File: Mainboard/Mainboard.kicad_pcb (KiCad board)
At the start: 2 copper layers, 60 x 84 mm, 27 parts, among them J1 Bus_M.2_Socket_E, J3 USB_A_Stacked, J4 Micro_SD_Card, J6 Conn_01x09_Pin, J7 Conn_01x09_Pin, U1 Hirose DF40C-100DS-0.4V, U2 ADS1115IDGS, U3 PCM5102, U4 PAM8403

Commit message: Second Commit (Test)
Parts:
- moved C4 10.8 mm to (88.8, 117.2)
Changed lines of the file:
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@@
 	(footprint "Capacitor_SMD:C_0201_0603Metric_Pad0.64x0.40mm_HandSolder"
 		(layer "F.Cu")
-		(at 80.156 123.753685)
+		(at 88.8175 117.25)
 		(descr "Capacitor SMD 0201 (0603 Metric), square (rectangular) end terminal, IPC-7351 nominal with elongated pad for handsoldering. (Body size source: https://www.vishay.com/docs/20052/crcw0201e3.pdf), generated with kicad-footprint-generator")
 		(tags "capacitor handsolder")

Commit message: Mini Resistor Update
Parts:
- moved R~{5.1kO}1 143.1 mm to (99.8, 124.9), turned to -90 degrees
- moved R~{5.1kO}2 139.6 mm to (101.5, 124.9), turned to -90 degrees
- moved R4.7kO3 85.4 mm to (146.7, 93.5)
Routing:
- net Net-(USBC_ALTPWR1-CC2): track 0.00 -> 4.41 mm
- net Net-(USBC_ALTPWR1-CC1): track 0.00 -> 4.09 mm
- net GND: track 0.00 -> 1.75 mm
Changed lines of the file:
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@@
 	(footprint "Resistor_SMD:R_0603_1608Metric_Pad0.98x0.95mm_HandSolder"
 		(layer "F.Cu")
-		(at 229.605 69.39)
+		(at 101.5 124.9125 -90)
 		(descr "Resistor SMD 0603 (1608 Metric), square (rectangular) end terminal, IPC-7351 nominal with elongated pad for handsoldering. (Body size source: IPC-SM-782 page 72, https://www.pcb-3d.com/wordpress/wp-content/uploads/ipc-sm-782a_amendment_1_and_2.pdf), generated with kicad-footprint-generator")
 		(tags "resistor handsolder")
 		(property "Reference" "R~{5.1kO}2"
-			(at 0 -1.43 0)
+			(at 2.8375 0 180)
 			(layer "F.SilkS")
 			(effects
@@
 		)
 		(property "Value" "R"
-			(at 0 1.43 0)
+			(at 0 1.43 90)
 			(layer "F.Fab")
+			(hide yes)
 			(effects
 				(font
@@
 		)
 		(property "Datasheet" ""
-			(at 0 0 0)
+			(at 0 0 90)
 			(layer "F.Fab")
 			(hide yes)
@@
 		)
 		(property "Description" "Resistor"
-			(at 0 0 0)
+			(at 0 0 90)
 			(layer "F.Fab")
 			(hide yes)
@@
 		(duplicate_pad_numbers_are_jumpers no)
 		(fp_line
-			(start -0.254724 -0.5225)
-			(end 0.254724 -0.5225)
+			(start -0.254724 0.5225)
+			(end 0.254724 0.5225)
 			(stroke
 				(width 0.12)
@@
 		)
 		(fp_line
-			(start -0.254724 0.5225)
-			(end 0.254724 0.5225)
+			(start -0.254724 -0.5225)
+			(end 0.254724 -0.5225)
 			(stroke
 				(width 0.12)
@@
 		)
 		(fp_line
-			(start -1.65 -0.73)
-			(end 1.65 -0.73)
+			(start -1.65 0.73)
+			(end -1.65 -0.73)
 			(stroke
 				(width 0.05)
@@
 		)
 		(fp_line
-			(start -1.65 0.73)
-			(end -1.65 -0.73)
+			(start 1.65 0.73)
+			(end -1.65 0.73)
 			(stroke
 				(width 0.05)
@@
 		)
 		(fp_line
-			(start 1.65 -0.73)
-			(end 1.65 0.73)
+			(start -1.65 -0.73)
+			(end 1.65 -0.73)
 			(stroke
 				(width 0.05)
@@
 		)
 		(fp_line
-			(start 1.65 0.73)
-			(end -1.65 0.73)
+			(start 1.65 -0.73)
+			(end 1.65 0.73)
 			(stroke
 				(width 0.05)
@@
 		)
 		(fp_line
-			(start -0.8 -0.4125)
-			(end 0.8 -0.4125)
+			(start -0.8 0.4125)
+			(end -0.8 -0.4125)
 			(stroke
 				(width 0.1)
@@
 		)
 		(fp_line
-			(start -0.8 0.4125)
-			(end -0.8 -0.4125)
+			(start 0.8 0.4125)
+			(end -0.8 0.4125)
 			(stroke
 				(width 0.1)
@@
 		)
 		(fp_line
-			(start 0.8 -0.4125)
-			(end 0.8 0.4125)
+			(start -0.8 -0.4125)
+			(end 0.8 -0.4125)
 			(stroke
 				(width 0.1)
@@
 		)
 		(fp_line
-			(start 0.8 0.4125)
-			(end -0.8 0.4125)
+			(start 0.8 -0.4125)
+			(end 0.8 0.4125)
 			(stroke
 				(width 0.1)
@@
 		)
 		(fp_text user "${REFERENCE}"
-			(at 0 0 0)
+			(at 0 0 90)
 			(layer "F.Fab")
 			(effects
@@
 		)
 		(pad "1" smd roundrect
-			(at -0.9125 0)
+			(at -0.9125 0 270)
 			(size 0.975 0.95)
 			(layers "F.Cu" "F.Mask" "F.Paste")
@@
 		)
 		(pad "2" smd roundrect
-			(at 0.9125 0)
+			(at 0.9125 0 270)
 			(size 0.975 0.95)
 			(layers "F.Cu" "F.Mask" "F.Paste")
@@
 	(footprint "Resistor_SMD:R_0603_1608Metric_Pad0.98x0.95mm_HandSolder"
 		(layer "F.Cu")
-		(at 230.75 78.75)
+		(at 146.6625 93.5)
 		(descr "Resistor SMD 0603 (1608 Metric), square (rectangular) end terminal, IPC-7351 nominal with elongated pad for handsoldering. (Body size source: IPC-SM-782 page 72, https://www.pcb-3d.com/wordpress/wp-content/uploads/ipc-sm-782a_amendment_1_and_2.pdf), generated with kicad-footprint-generator")
 		(tags "resistor handsolder")
@@
 	(footprint "Resistor_SMD:R_0603_1608Metric_Pad0.98x0.95mm_HandSolder"
 		(layer "F.Cu")
-		(at 229.605 64.75)
+		(at 99.75 124.9125 -90)
 		(descr "Resistor SMD 0603 (1608 Metric), square (rectangular) end terminal, IPC-7351 nominal with elongated pad for handsoldering. (Body size source: IPC-SM-782 page 72, https://www.pcb-3d.com/wordpress/wp-content/uploads/ipc-sm-782a_amendment_1_and_2.pdf), generated with kicad-footprint-generator")
 		(tags "resistor handsolder")
 		(property "Reference" "R~{5.1kO}1"
-			(at 0 -1.43 0)
+			(at -2.5875 1 180)
 			(layer "F.SilkS")
 			(effects
@@
 		)
 		(property "Value" "R"
-			(at 0 1.43 0)
+			(at 0 1.43 90)
 			(layer "F.Fab")
+			(hide yes)
 			(effects
 				(font
@@
 		)
 		(property "Datasheet" ""
-			(at 0 0 0)
+			(at 0 0 90)
 			(layer "F.Fab")
 			(hide yes)
@@
 		)
 		(property "Description" "Resistor"
-			(at 0 0 0)
+			(at 0 0 90)
 			(layer "F.Fab")
 			(hide yes)
@@
 		(duplicate_pad_numbers_are_jumpers no)
 		(fp_line
-			(start -0.254724 -0.5225)
-			(end 0.254724 -0.5225)
+			(start -0.254724 0.5225)
+			(end 0.254724 0.5225)
 			(stroke
 				(width 0.12)
@@
 		)
 		(fp_line
-			(start -0.254724 0.5225)
-			(end 0.254724 0.5225)
+			(start -0.254724 -0.5225)
+			(end 0.254724 -0.5225)
 			(stroke
 				(width 0.12)
@@
 		)
 		(fp_line
-			(start -1.65 -0.73)
-			(end 1.65 -0.73)
+			(start -1.65 0.73)
+			(end -1.65 -0.73)
 			(stroke
 				(width 0.05)
@@
 		)
 		(fp_line
-			(start -1.65 0.73)
-			(end -1.65 -0.73)
+			(start 1.65 0.73)
+			(end -1.65 0.73)
 			(stroke
 				(width 0.05)
@@
 		)
 		(fp_line
-			(start 1.65 -0.73)
-			(end 1.65 0.73)
+			(start -1.65 -0.73)
+			(end 1.65 -0.73)
 			(stroke
 				(width 0.05)
@@
 		)
 		(fp_line
-			(start 1.65 0.73)
-			(end -1.65 0.73)
+			(start 1.65 -0.73)
+			(end 1.65 0.73)
 			(stroke
 				(width 0.05)
@@
 		)
 		(fp_line
-			(start -0.8 -0.4125)
-			(end 0.8 -0.4125)
+			(start -0.8 0.4125)
+			(end -0.8 -0.4125)
 			(stroke
 				(width 0.1)
@@
 		)
 		(fp_line
-			(start -0.8 0.4125)
-			(end -0.8 -0.4125)
+			(start 0.8 0.4125)
+			(end -0.8 0.4125)
 			(stroke
 				(width 0.1)
@@
 		)
 		(fp_line
-			(start 0.8 -0.4125)
-			(end 0.8 0.4125)
+			(start -0.8 -0.4125)
+			(end 0.8 -0.4125)
 			(stroke
 				(width 0.1)
@@
 		)
 		(fp_line
-			(start 0.8 0.4125)
-			(end -0.8 0.4125)
+			(start 0.8 -0.4125)
+			(end 0.8 0.4125)
 			(stroke
 				(width 0.1)
@@
 		)
 		(fp_text user "${REFERENCE}"
-			(at 0 0 0)
+			(at 0 0 90)
 			(layer "F.Fab")
 			(effects
@@
 		)
 		(pad "1" smd roundrect
-			(at -0.9125 0)
+			(at -0.9125 0 270)
 			(size 0.975 0.95)
 			(layers "F.Cu" "F.Mask" "F.Paste")
@@
 		)
 		(pad "2" smd roundrect
-			(at 0.9125 0)
+			(at 0.9125 0 270)
 			(size 0.975 0.95)
 			(layers "F.Cu" "F.Mask" "F.Paste")
@@
 		(net "/3V3")
 	)
+	(segment
+		(start 99.75 125.825)
+		(end 99.75 129.92)
+		(width 0.2)
+		(layer "F.Cu")
+		(net "Net-(USBC_ALTPWR1-CC1)")
+	)
+	(segment
+		(start 101.5 124)
+		(end 99.75 124)
+		(width 0.2)
+		(layer "F.Cu")
+		(net "GND")
+	)
+	(segment
+		(start 101.5 125.825)
+		(end 100.75 126.575)
+		(width 0.2)
+		(layer "F.Cu")
+		(net "Net-(USBC_ALTPWR1-CC2)")
+	)
+	(segment
+		(start 100.75 126.575)
+		(end 100.75 129.92)
+		(width 0.2)
+		(layer "F.Cu")
+		(net "Net-(USBC_ALTPWR1-CC2)")
+	)
 	(embedded_fonts no)

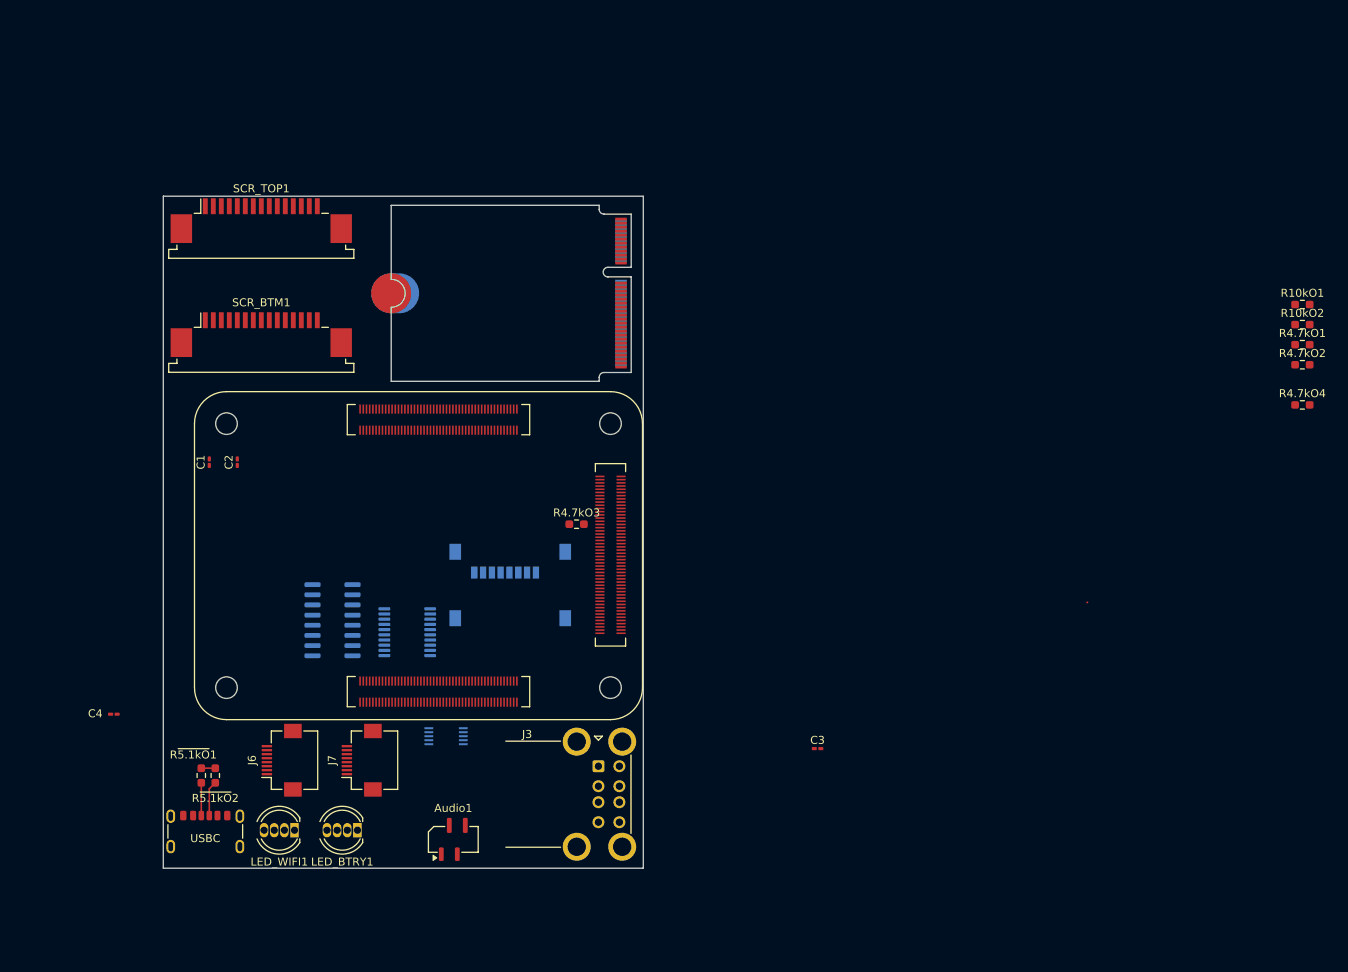
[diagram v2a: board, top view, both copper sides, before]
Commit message: New larger layout size (PCB)
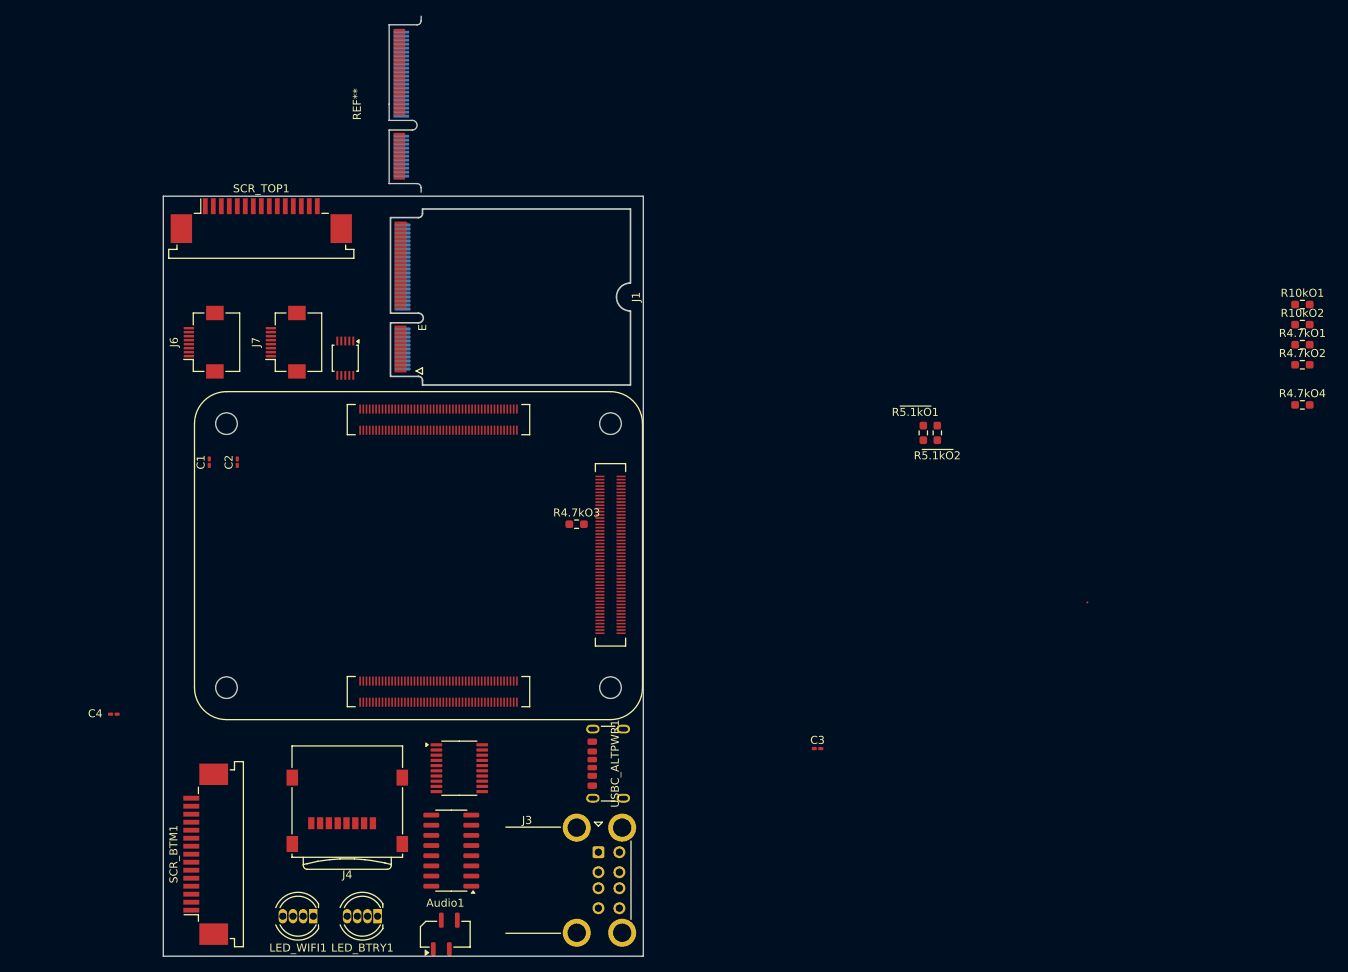
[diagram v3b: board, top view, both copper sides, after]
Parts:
- added REF**: NGFF_E, NGFF:NGFF_E, F.Cu at (123.2, 41.0)
- J1: footprint M.2_2230_E:2230-key-E -> Connector_PCBEdge:M.2_2230-xx-E
- J4, U2, U3: moved to F.Cu
- U4: value PAM8403 -> PAM8403D; moved to F.Cu
- moved R~{5.1kO}1 99.9 mm to (190.0, 82.1)
- moved R~{5.1kO}2 99.9 mm to (191.8, 82.1)
- moved SCR_BTM1 65.3 mm to (100.3, 134.8), turned to 90 degrees
- moved J6 53.2 mm to (100.0, 70.8)
- moved J7 53.1 mm to (110.3, 70.8)
- moved USBC_ALTPWR1 52.3 mm to (151.7, 123.4), turned to 90 degrees
- moved U2 48.9 mm to (117.8, 72.8), turned to -90 degrees
- moved J4 34.8 mm to (118.0, 129.3)
- moved U4 32.4 mm to (131.0, 134.3)
- moved U3 18.2 mm to (132.0, 124.0), turned to 0 degrees
- moved J1 12.5 mm to (127.4, 65.1), turned to -90 degrees
- moved Audio1 11.9 mm to (130.2, 144.8)
- moved LED_BTRY1 11.0 mm to (121.8, 142.5)
- moved LED_WIFI1 11.0 mm to (113.8, 142.5)
- moved J3 10.8 mm to (149.4, 134.5)
- renumbered USBC to USBC_ALTPWR1
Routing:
- net Net-(USBC_ALTPWR1-CC2): track 4.41 -> 0.00 mm
- net Net-(USBC_ALTPWR1-CC1): track 4.09 -> 0.00 mm
- net GND: track 1.75 -> 0.81 mm
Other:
- board size 60 x 84 mm -> 60 x 95 mm

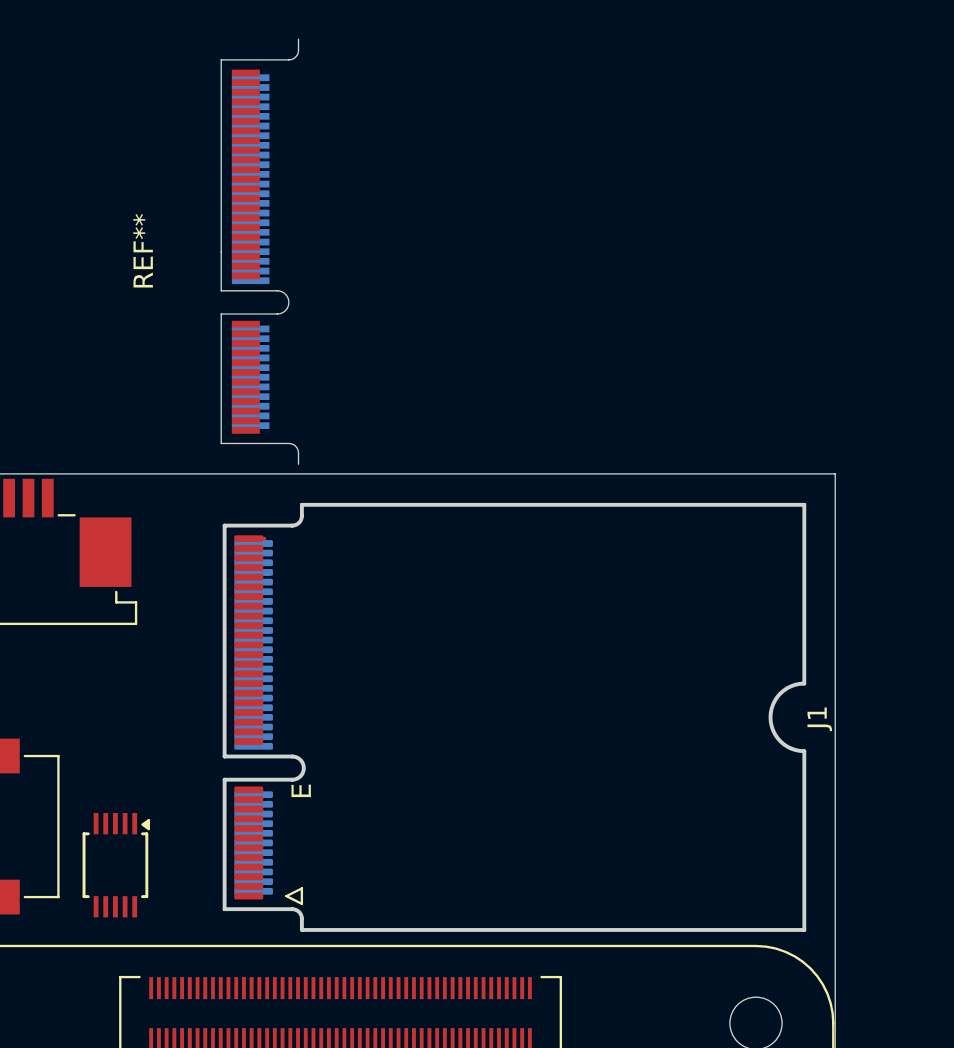
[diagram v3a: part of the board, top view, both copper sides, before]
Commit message: Fixed M.2 Connector Setup
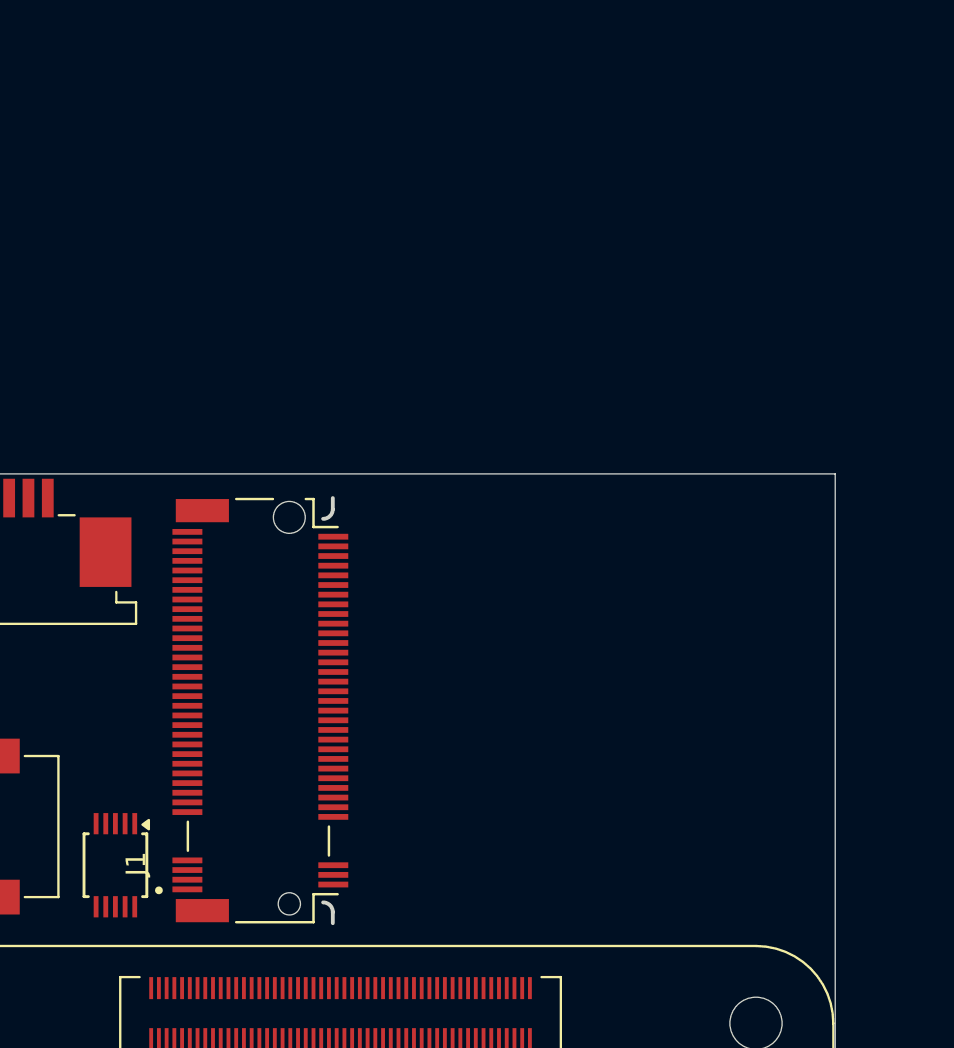
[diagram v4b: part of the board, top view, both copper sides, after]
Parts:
- removed the REF** at (123.2, 41.0)
- added REF**: M.2_2230_E_Frame, Connector_PCBEdge:M.2_2230_E_Frame, F.Cu at (129.0, 64.8)
- J1: footprint Connector_PCBEdge:M.2_2230-xx-E -> 2199230-8:TE_2199230-8
- moved J1 0.74 mm to (126.8, 64.8), turned to 90 degrees
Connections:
- R4.7kO3 pad 1: unconnected-(R4.7kO3-Pad1) -> /3V3
- R4.7kO4 pad 1: unconnected-(R4.7kO4-Pad1) -> /3V3
- R4.7kO4 pad 2: /3V3 -> Net-(SCR_BTM1-Pin_12)
- SCR_BTM1 pad 12: /3V3 -> Net-(SCR_BTM1-Pin_12)
- SCR_TOP1 pad 12: /3V3 -> Net-(SCR_BTM1-Pin_12)
- U1 pad 271: /3V3 -> Net-(SCR_BTM1-Pin_12)
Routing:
- net GND: track 0.81 -> 0.00 mm

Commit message: Routed Wifi; USB_D, TX and RX Dfpairs
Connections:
- net Net-(J1-PERn0) renamed /PER-
- net Net-(J1-PERp0) renamed /PER+
- net Net-(J1-PETn0) renamed /PET-
- net Net-(J1-PETp0) renamed /PET+
- net Net-(J1-USB_D+) renamed /Wifi+
- net Net-(J1-USB_D-) renamed /Wifi-
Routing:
- net /3V3: track 0.11 -> 20.3 mm
- net /PER-: track 0.00 -> 18.5 mm, vias 0 -> 2
- net /PER+: track 0.00 -> 18.2 mm, vias 0 -> 2
- net /PET-: track 0.00 -> 16.6 mm
- net /PET+: track 0.00 -> 16.6 mm
- net GND: track 0.00 -> 16.2 mm
- net /Wifi-: track 0.00 -> 12.4 mm
- net /Wifi+: track 0.00 -> 12.4 mm
- net Net-(J1-~{LED_1}): track 0.00 -> 1.01 mm, vias 0 -> 1
